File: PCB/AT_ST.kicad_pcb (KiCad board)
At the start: 2 copper layers, 127.3 x 96.8 mm, 84 parts, among them J1 4PIN, J2 OLED, J3 Conn_01x05_Female, J4 Conn_01x05_Female, SW1 SW1, SW10 SW10, SW11 SW11, SW12 SW12, SW13 SW13, SW14 SW14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

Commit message: Some more changes.
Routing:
- net GND: track 20.6 -> 21.1 mm
- net row2: vias 3 -> 2

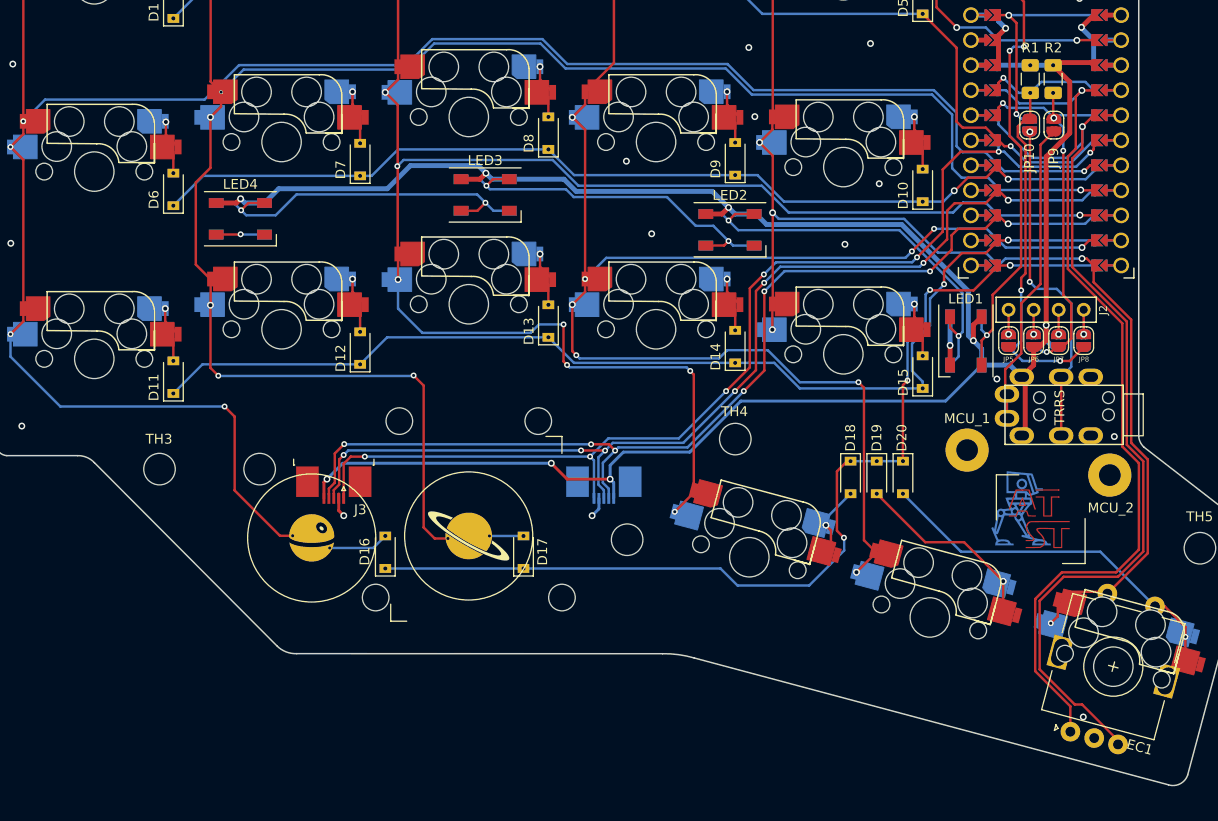
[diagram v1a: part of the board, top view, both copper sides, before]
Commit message: Updated some footprints.
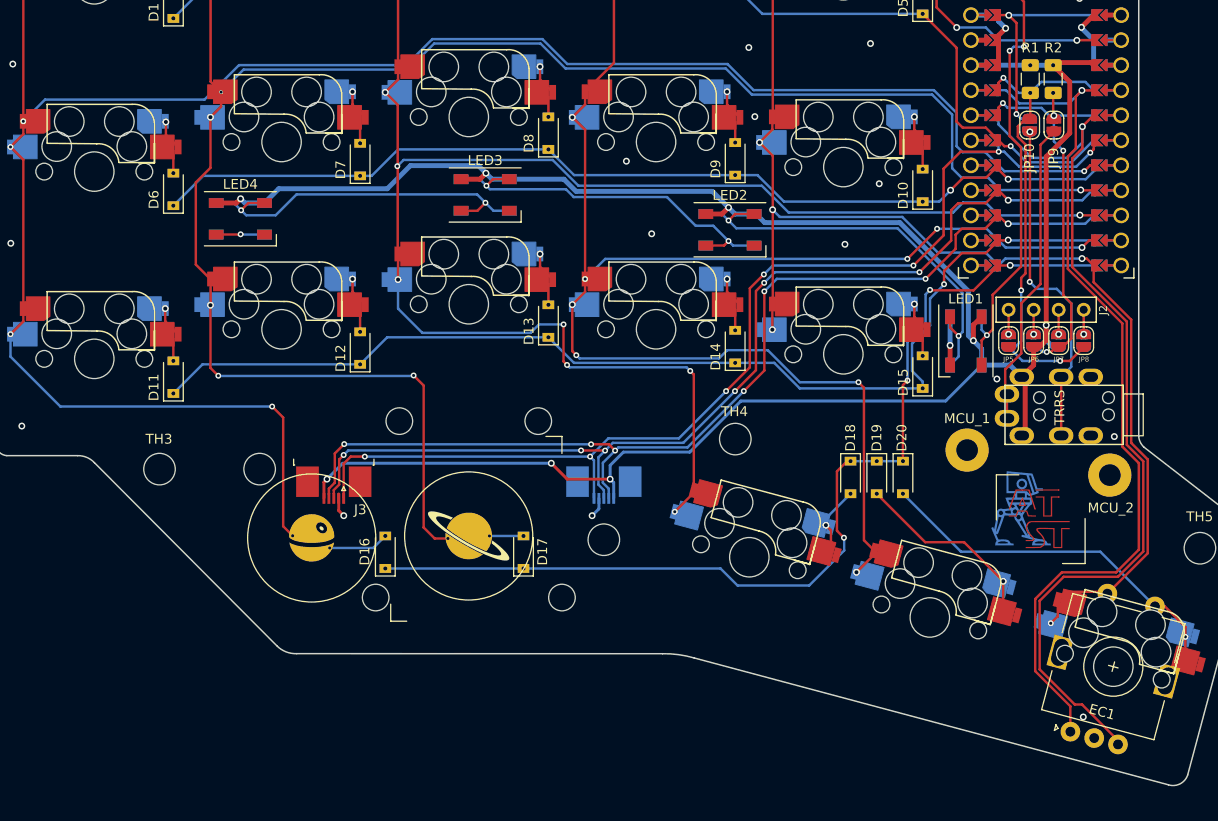
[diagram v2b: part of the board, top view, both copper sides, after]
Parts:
- R1, R2: footprint SofleKeyboard-footprint:R_1206_DoubleSided -> jw_custom_footprint:R_1206_DoubleSided
- moved JY_BT_2 2.36 mm to (159.6, 130.4)
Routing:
- net col0: track 205.9 -> 208.0 mm
